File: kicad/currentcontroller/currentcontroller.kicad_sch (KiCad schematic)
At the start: 33 parts

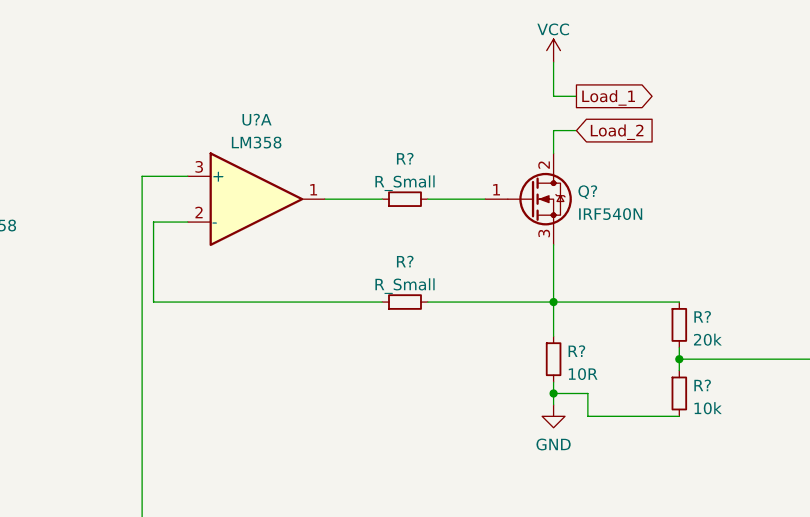
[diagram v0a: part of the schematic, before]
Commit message: Adjusted to other DAC
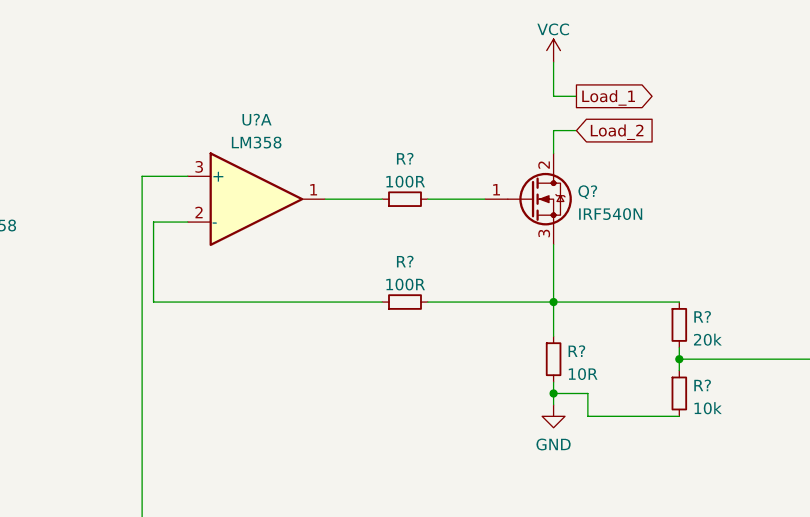
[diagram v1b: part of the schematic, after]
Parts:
- R? (x2): value R_Small -> 100R
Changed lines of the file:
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@@
     (in_bom yes) (on_board yes) (fields_autoplaced)
     (property "Reference" "R?" (id 0) (at 96.52 41.2836 90))
-    (property "Value" "R_Small" (id 1) (at 96.52 43.8205 90))
+    (property "Value" "100R" (id 1) (at 96.52 43.8205 90))
     (property "Footprint" "" (id 2) (at 96.52 45.72 0)
       (effects (font (size 1.27 1.27)) hide)
@@
     (in_bom yes) (on_board yes) (fields_autoplaced)
     (property "Reference" "R?" (id 0) (at 96.52 52.7136 90))
-    (property "Value" "R_Small" (id 1) (at 96.52 55.2505 90))
+    (property "Value" "100R" (id 1) (at 96.52 55.2505 90))
     (property "Footprint" "" (id 2) (at 96.52 57.15 0)
       (effects (font (size 1.27 1.27)) hide)
@@
     )
     (path "/3db3fc00-95e4-4f1b-b3a5-5adfdb32b1bd"
-      (reference "R?") (unit 1) (value "R_Small") (footprint "")
+      (reference "R?") (unit 1) (value "100R") (footprint "")
     )
     (path "/4c9cff51-6d52-4202-bbc9-dbd5b4b813fb"
@@
     )
     (path "/8babeafd-266b-4398-9be4-8b65502efc0f"
-      (reference "R?") (unit 1) (value "R_Small") (footprint "")
+      (reference "R?") (unit 1) (value "100R") (footprint "")
     )
     (path "/98b3911b-db95-4c27-a110-f1819e71215e"

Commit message: Reflecting latest changes on PCB
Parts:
- removed R?: 20k, symbol Device:R_Small
- removed R?: 10k, symbol Device:R_Small
- added R?: 200R, symbol Device:R_Small
- gave numbers to parts that had none: 30
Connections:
- net at Q1.3 (S), R4.2, R6.1: now also U5.23 (PC0)
- net at J1.4 (Pin_4), U3.3: now also R?.2
- net at J1.1 (Pin_1), R9.2: now also R?.1

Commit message: Minor updates and finished PCB
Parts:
- removed U5: ATmega328P-A, Package_QFP:TQFP-32_7x7mm_P0.8mm, symbol MCU_Microchip_ATmega:ATmega328P-A
- added J3: Conn_01x02, Connector_PinHeader_2.54mm:PinHeader_1x02_P2.54mm_Horizontal, symbol Connector_Generic:Conn_01x02
- added J4: Conn_01x04, Connector_PinHeader_2.54mm:PinHeader_1x04_P2.54mm_Horizontal, symbol Connector_Generic:Conn_01x04
- added R7: 1M, Resistor_THT:R_Axial_DIN0309_L9.0mm_D3.2mm_P12.70mm_Horizontal, symbol Device:R_Small
- added U?: ATmega328P-P, Package_DIP:DIP-28_W7.62mm, symbol MCU_Microchip_ATmega:ATmega328P-P
- C1, C3, C4, C5, C6, C7: footprint (none) -> Capacitor_THT:C_Rect_L7.0mm_W2.0mm_P5.00mm
- C2, C8: footprint (none) -> Capacitor_THT:CP_Radial_D5.0mm_P2.50mm
- D1: footprint (none) -> LED_THT:LED_D5.0mm
- J1: footprint (none) -> Connector_PinHeader_2.54mm:PinHeader_1x04_P2.54mm_Horizontal
- J2: footprint (none) -> Connector_PinHeader_2.54mm:PinHeader_2x03_P2.54mm_Vertical
- R1, R10, R11, R12, R13, R2, R3, R4, R5, R6, R9: footprint (none) -> Resistor_THT:R_Axial_DIN0309_L9.0mm_D3.2mm_P12.70mm_Horizontal
- R8: renamed from R?; footprint (none) -> Resistor_THT:R_Axial_DIN0309_L9.0mm_D3.2mm_P12.70mm_Horizontal
- U1: footprint (none) -> Package_DIP:DIP-8_W7.62mm
- U2: footprint (none) -> Package_SO:MSOP-8_3x3mm_P0.65mm
- Y1: footprint (none) -> Connector_PinHeader_2.54mm:PinHeader_1x03_P2.54mm_Vertical
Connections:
- net +5V: now also J3.2 (Pin_2), U?.20 (AVCC), U?.7 (VCC)
- net GND: now also Y1.2, J3.1 (Pin_1), J4.1 (Pin_1), R7.1, U?.22 (GND), U?.8 (GND)
- net Load_2: now also J4.3 (Pin_3)
- net VCC: now also J4.2 (Pin_2), J4.4 (Pin_4)
- net at C5.1: now also U?.21 (AREF)
- net at R2.1, U2.2 (~{CS}): now also U?.5 (PD3)
- net at J2.4 (Pin_4), U2.4 (SDI): now also U?.17 (PB3)
- net at J2.1 (Pin_1): now also U?.18 (PB4)
- net at J2.3 (Pin_3), U2.3 (SCK): now also U?.19 (PB5)
- net at Q1.3 (S), R4.2, R6.1: now also U?.23 (PC0)
- net at C7.1, J2.5 (Pin_5), R11.2: now also U?.1 (~{RESET}/PC6)
- net at R10.1, U4.3: now also U?.2 (PD0)
- net at U3.1: now also U?.3 (PD1)
- net at U2.5 (~{LDAC}): now also U?.4 (PD2)
- net at Y1.3: now also U?.9 (XTAL1/PB6)
- net at Y1.1: now also U?.10 (XTAL2/PB7)
- net at Q1.1 (G), R3.2: now also R7.2
